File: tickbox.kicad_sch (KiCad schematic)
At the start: 27 parts, among them IC1 R5F10RLAGFB#10, J1 Conn_01x03_Socket, Q1 BC848, SW1 SW_MEC_5G, SW2 SW_MEC_5G, SW3 SW_MEC_5G, Y1 32.768 kHz

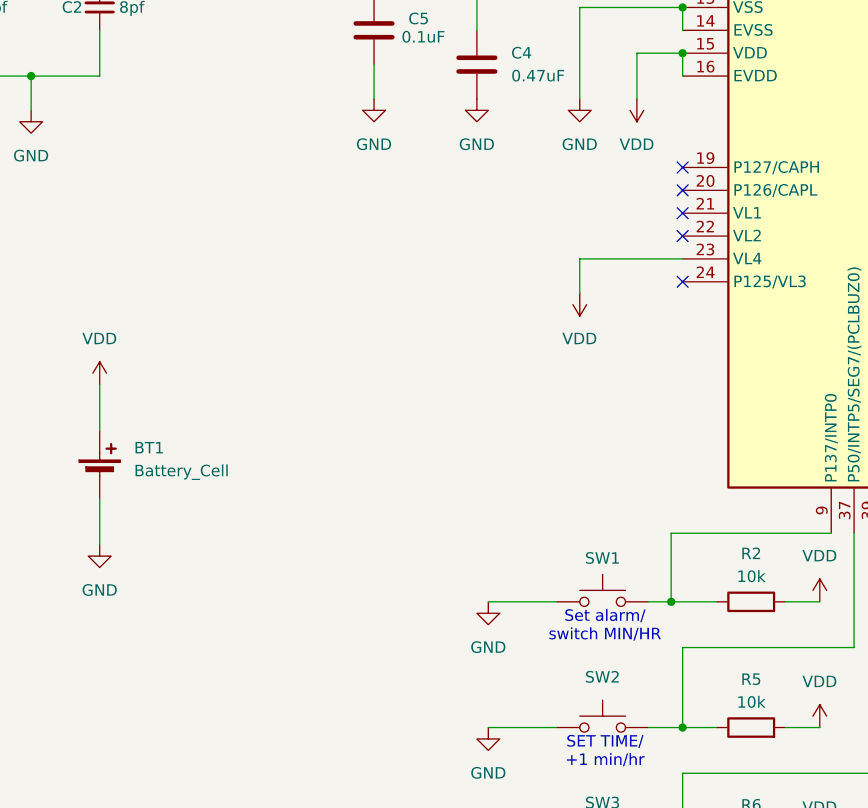
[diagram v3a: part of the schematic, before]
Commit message: added alarm switch
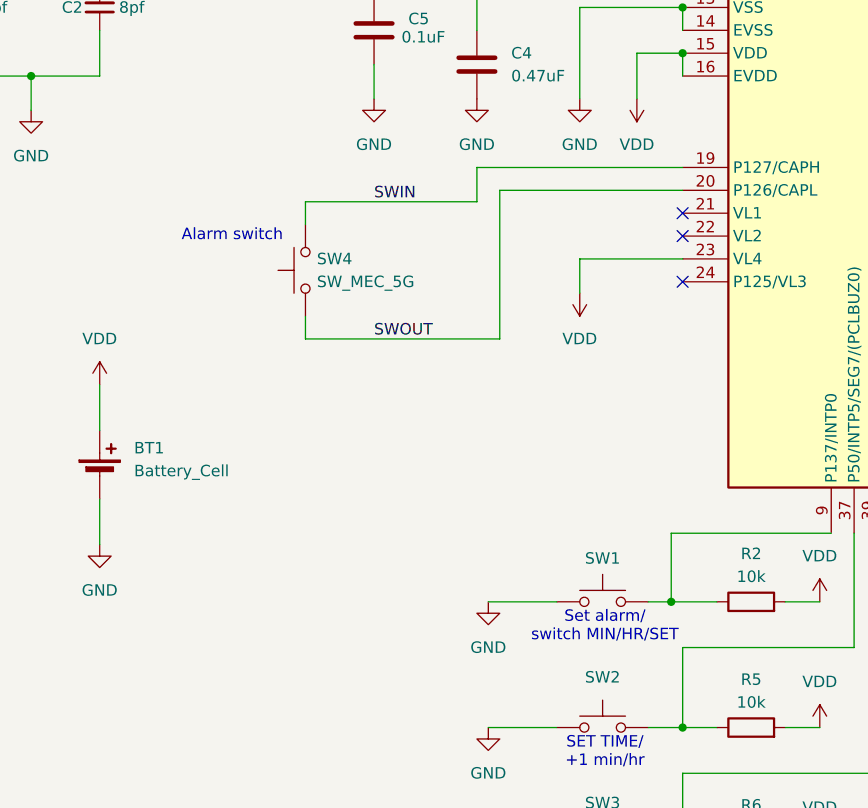
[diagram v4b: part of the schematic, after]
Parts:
- added SW4: SW_MEC_5G, symbol Switch:SW_MEC_5G
- BZ1: footprint (none) -> Buzzer_Beeper:Buzzer_TDK_PS1240P02BT_D12.2mm_H6.5mm
- Y1: footprint (none) -> Crystal:Crystal_DS26_D2.0mm_L6.0mm_Vertical
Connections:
- net SWIN: now reaches IC1.19 (P127/CAPH)
- net SWIN: now also SW4.3 (B), SW4.4 (B)
- net SWOUT: now reaches IC1.20 (P126/CAPL)
- net SWOUT: now also SW4.1 (A), SW4.2 (A)
- no-connect marks 7 -> 5
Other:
- note added: "Alarm switch"
- note added: "Set alarm/ switch MIN/HR/SET"
- note removed: "Set alarm/ switch MIN/HR"
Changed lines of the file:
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@@
 		)
 	)
+	(text "Alarm switch"
+		(exclude_from_sim no)
+		(at 49.022 111.76 0)
+		(effects
+			(font
+				(size 1.27 1.27)
+			)
+		)
+	)
 	(text "LCD backlight"
 		(exclude_from_sim no)
@@
 		)
 	)
-	(text "Set alarm/\nswitch MIN/HR"
+	(text "Set alarm/\nswitch MIN/HR/SET"
 		(exclude_from_sim no)
 		(at 90.424 155.194 0)
@@
 	)
 	(no_connect
-		(at 99.06 106.68)
-	)
-	(no_connect
 		(at 160.02 36.83)
 	)
@@
 	)
 	(no_connect
-		(at 99.06 104.14)
-	)
-	(no_connect
 		(at 99.06 109.22)
 	)
@@
 	(wire
 		(pts
+			(xy 76.2 104.14) (xy 99.06 104.14)
+		)
+		(stroke
+			(width 0)
+			(type default)
+		)
+	)
+	(wire
+		(pts
 			(xy 154.94 151.13) (xy 154.94 149.86)
 		)
@@
 	(wire
 		(pts
+			(xy 78.74 106.68) (xy 99.06 106.68)
+		)
+		(stroke
+			(width 0)
+			(type default)
+		)
+	)
+	(wire
+		(pts
 			(xy 256.54 105.41) (xy 256.54 113.03)
 		)
@@
 	(wire
 		(pts
+			(xy 57.15 110.49) (xy 57.15 107.95)
+		)
+		(stroke
+			(width 0)
+			(type default)
+		)
+	)
+	(wire
+		(pts
 			(xy 92.71 58.42) (xy 99.06 58.42)
 		)
@@
 	(wire
 		(pts
+			(xy 76.2 104.14) (xy 76.2 107.95)
+		)
+		(stroke
+			(width 0)
+			(type default)
+		)
+	)
+	(wire
+		(pts
 			(xy 251.46 64.77) (xy 251.46 72.39)
 		)
@@
 	(wire
 		(pts
+			(xy 57.15 120.65) (xy 57.15 123.19)
+		)
+		(stroke
+			(width 0)
+			(type default)
+		)
+	)
+	(wire
+		(pts
 			(xy 218.44 105.41) (xy 218.44 113.03)
 		)
@@
 		)
 	)
+	(wire
+		(pts
+			(xy 78.74 106.68) (xy 78.74 123.19)
+		)
+		(stroke
+			(width 0)
+			(type default)
+		)
+	)
 	(bus
 		(pts
@@
 	(wire
 		(pts
+			(xy 57.15 107.95) (xy 76.2 107.95)
+		)
+		(stroke
+			(width 0)
+			(type default)
+		)
+	)
+	(wire
+		(pts
 			(xy 45.72 34.29) (xy 45.72 36.83)
 		)
@@
 	(wire
 		(pts
+			(xy 57.15 123.19) (xy 78.74 123.19)
+		)
+		(stroke
+			(width 0)
+			(type default)
+		)
+	)
+	(wire
+		(pts
 			(xy 26.67 93.98) (xy 26.67 97.79)
 		)
@@
 		)
 	)
+	(label "SWIN"
+		(at 64.77 107.95 0)
+		(effects
+			(font
+				(size 1.27 1.27)
+			)
+			(justify left bottom)
+		)
+	)
 	(label "SEG18"
 		(at 187.96 92.71 0)
@@
 		)
 	)
+	(label "SWOUT"
+		(at 64.77 123.19 0)
+		(effects
+			(font
+				(size 1.27 1.27)
+			)
+			(justify left bottom)
+		)
+	)
 	(label "SEG24"
 		(at 187.96 107.95 0)
@@
 	)
 	(symbol
+		(lib_id "Switch:SW_MEC_5G")
+		(at 57.15 115.57 90)
+		(unit 1)
+		(exclude_from_sim no)
+		(in_bom yes)
+		(on_board yes)
+		(dnp no)
+		(fields_autoplaced yes)
+		(property "Reference" "SW4"
+			(at 58.42 114.2999 90)
+			(effects
+				(font
+					(size 1.27 1.27)
+				)
+				(justify right)
+			)
+		)
+		(property "Value" "SW_MEC_5G"
+			(at 58.42 116.8399 90)
+			(effects
+				(font
+					(size 1.27 1.27)
+				)
+				(justify right)
+			)
+		)
+		(property "Footprint" ""
+			(at 52.07 115.57 0)
+			(effects
+				(font
+					(size 1.27 1.27)
+				)
+				(hide yes)
+			)
+		)
+		(property "Datasheet" "http://www.apem.com/int/index.php?controller=attachment&id_attachment=488"
+			(at 52.07 115.57 0)
+			(effects
+				(font
+					(size 1.27 1.27)
+				)
+				(hide yes)
+			)
+		)
+		(property "Description" "MEC 5G single pole normally-open tactile switch"
+			(at 57.15 115.57 0)
+			(effects
+				(font
+					(size 1.27 1.27)
+				)
+				(hide yes)
+			)
+		)
+		(pin "2"
+		)
+		(pin "1"
+		)
+		(pin "3"
+		)
+		(pin "4"
+		)
+		(instances
+			(project ""
+				(path "/1b82f5d3-e703-47bd-a7eb-0d448666d009"
+					(reference "SW4")
+					(unit 1)
+				)
+			)
+		)
+	)
+	(symbol
 		(lib_id "power:GND")
 		(at 64.77 96.52 0)
@@
 			)
 		)
-		(property "Footprint" ""
+		(property "Footprint" "Crystal:Crystal_DS26_D2.0mm_L6.0mm_Vertical"
 			(at 26.67 80.01 0)
 			(effects
@@
 			)
 		)
-		(property "Footprint" ""
+		(property "Footprint" "Buzzer_Beeper:Buzzer_TDK_PS1240P02BT_D12.2mm_H6.5mm"
 			(at 165.735 154.94 90)
 			(effects

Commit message: Sketch PCB layout
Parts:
- removed J1: Conn_01x03_Socket, symbol Connector:Conn_01x03_Socket
- added J1: Conn_01x03_Pin, Connector_PinHeader_2.54mm:PinHeader_1x03_P2.54mm_Vertical, symbol Connector:Conn_01x03_Pin
- added J2: Conn_01x02_Pin, Connector_PinHeader_2.54mm:PinHeader_1x02_P2.54mm_Vertical, symbol Connector:Conn_01x02_Pin
- C1, C2, C4, C5: footprint (none) -> Capacitor_SMD:C_1206_3216Metric_Pad1.33x1.80mm_HandSolder
- D2: footprint (none) -> LED_SMD:LED_1206_3216Metric_Pad1.42x1.75mm_HandSolder
- R1: value 1k -> 10k; footprint (none) -> Resistor_SMD:R_1206_3216Metric_Pad1.30x1.75mm_HandSolder
- R10, R11, R12, R13, R2, R4, R5, R6, R7, R9: footprint (none) -> Resistor_SMD:R_1206_3216Metric_Pad1.30x1.75mm_HandSolder
- R3: value 10k -> 1k; footprint (none) -> Resistor_SMD:R_1206_3216Metric_Pad1.30x1.75mm_HandSolder
- SW1, SW2, SW3: footprint (none) -> Button_Switch_THT:SW_SPST_Omron_B3F-315x_Angled
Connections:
- net SEG17 is gone; now on net SEG1: D1.22 (4F)
- net GND: now also J2.1 (Pin_1)
- net RESET: now also R3.2, J1.3 (Pin_3); no longer R1.2
- net SEG0: now also D1.21 (4A); no longer D1.37 (1G)
- net SEG1: no longer D1.36 (1F)
- net SEG10: now also D1.28 (COL); no longer D1.29 (2B)
- net SEG11: now also D1.29 (2B); no longer D1.28 (COL)
- net SEG12: now also D1.30 (2A); no longer D1.27 (3G)
- net SEG13: now also D1.31 (2F); no longer D1.26 (3F)
- net SEG14: now also D1.32 (2G); no longer D1.25 (3A)
- net SEG15: now also D1.34 (1B); no longer D1.24 (3B)
- net SEG16: now also D1.35 (1A); no longer D1.23 (4G)
- net SEG18: now also D1.36 (1F); no longer D1.21 (4A)
- net SEG19: now also D1.37 (1G)
- net SEG2: now also D1.23 (4G); no longer D1.35 (1A)
- net SEG3: now also D1.24 (3B); no longer D1.34 (1B)
- net SEG6: now also D1.25 (3A); no longer D1.32 (2G)
- net SEG8: now also D1.26 (3F); no longer D1.31 (2F)
- net SEG9: now also D1.27 (3G); no longer D1.30 (2A)
- net TOOLRXD: now also R12.2, J1.2 (Pin_2); no longer R3.2
- net TOOLTXD: now also R1.2, J1.1 (Pin_1); no longer R12.2
- net VDD: now also J2.2 (Pin_2)
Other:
- moved on the sheet: R1, R12, R3, R4

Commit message: add coin holder etc
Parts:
- SW4: footprint (none) -> 3rdparty:Wire_pads
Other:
- moved on the sheet: C5
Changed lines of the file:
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@@
 	(wire
 		(pts
-			(xy 64.77 81.28) (xy 64.77 85.09)
+			(xy 21.59 129.54) (xy 21.59 133.35)
 		)
 		(stroke
@@
 	(wire
 		(pts
-			(xy 64.77 92.71) (xy 64.77 96.52)
+			(xy 21.59 140.97) (xy 21.59 144.78)
 		)
 		(stroke
@@
 			)
 		)
-		(property "Footprint" ""
+		(property "Footprint" "3rdparty:Wire_pads"
 			(at 52.07 115.57 0)
 			(effects
@@
 	(symbol
 		(lib_id "power:GND")
-		(at 64.77 96.52 0)
+		(at 21.59 144.78 0)
 		(unit 1)
 		(exclude_from_sim no)
@@
 		(fields_autoplaced yes)
 		(property "Reference" "#PWR06"
-			(at 64.77 102.87 0)
+			(at 21.59 151.13 0)
 			(effects
 				(font
@@
 		)
 		(property "Value" "GND"
-			(at 64.77 101.6 0)
+			(at 21.59 149.86 0)
 			(effects
 				(font
@@
 		)
 		(property "Footprint" ""
-			(at 64.77 96.52 0)
+			(at 21.59 144.78 0)
 			(effects
 				(font
@@
 		)
 		(property "Datasheet" ""
-			(at 64.77 96.52 0)
+			(at 21.59 144.78 0)
 			(effects
 				(font
@@
 		)
 		(property "Description" "Power symbol creates a global label with name \"GND\" , ground"
-			(at 64.77 96.52 0)
+			(at 21.59 144.78 0)
 			(effects
 				(font
@@
 	(symbol
 		(lib_id "Device:C")
-		(at 64.77 88.9 0)
+		(at 21.59 137.16 0)
 		(unit 1)
 		(exclude_from_sim no)
@@
 		(dnp no)
 		(property "Reference" "C5"
-			(at 68.58 87.6299 0)
+			(at 25.4 135.8899 0)
 			(effects
 				(font
@@
 		)
 		(property "Value" "0.1uF"
-			(at 67.818 89.662 0)
+			(at 24.638 137.922 0)
 			(effects
 				(font
@@
 		)
 		(property "Footprint" "Capacitor_SMD:C_1206_3216Metric_Pad1.33x1.80mm_HandSolder"
-			(at 65.7352 92.71 0)
+			(at 22.5552 140.97 0)
 			(effects
 				(font
@@
 		)
 		(property "Datasheet" "~"
-			(at 64.77 88.9 0)
+			(at 21.59 137.16 0)
 			(effects
 				(font
@@
 		)
 		(property "Description" "Unpolarized capacitor"
-			(at 64.77 88.9 0)
+			(at 21.59 137.16 0)
 			(effects
 				(font
@@
 	(symbol
 		(lib_id "power:VDD")
-		(at 64.77 81.28 0)
+		(at 21.59 129.54 0)
 		(unit 1)
 		(exclude_from_sim no)
@@
 		(fields_autoplaced yes)
 		(property "Reference" "#PWR05"
-			(at 64.77 85.09 0)
+			(at 21.59 133.35 0)
 			(effects
 				(font
@@
 		)
 		(property "Value" "VDD"
-			(at 64.77 76.2 0)
+			(at 21.59 124.46 0)
 			(effects
 				(font
@@
 		)
 		(property "Footprint" ""
-			(at 64.77 81.28 0)
+			(at 21.59 129.54 0)
 			(effects
 				(font
@@
 		)
 		(property "Datasheet" ""
-			(at 64.77 81.28 0)
+			(at 21.59 129.54 0)
 			(effects
 				(font
@@
 		)
 		(property "Description" "Power symbol creates a global label with name \"VDD\""
-			(at 64.77 81.28 0)
+			(at 21.59 129.54 0)
 			(effects
 				(font
